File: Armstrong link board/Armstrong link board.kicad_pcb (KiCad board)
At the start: 2 copper layers, 32 x 28 mm, 8 parts, among them J1 Camera, J2 Wheelson, J3 Armstrong, J4 Conn_01x03_Pin, J5 JST 2.0, J6 USB_C_Receptacle_USB2.0_16P

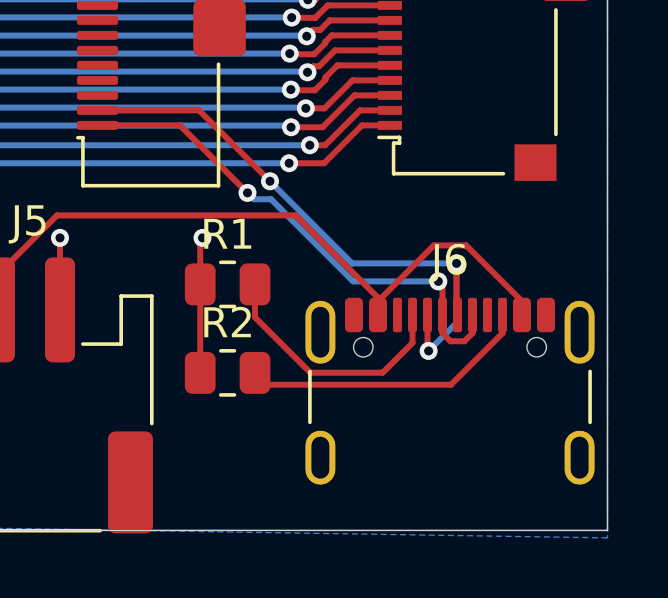
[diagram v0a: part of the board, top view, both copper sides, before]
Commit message: connect ground and shield from usb
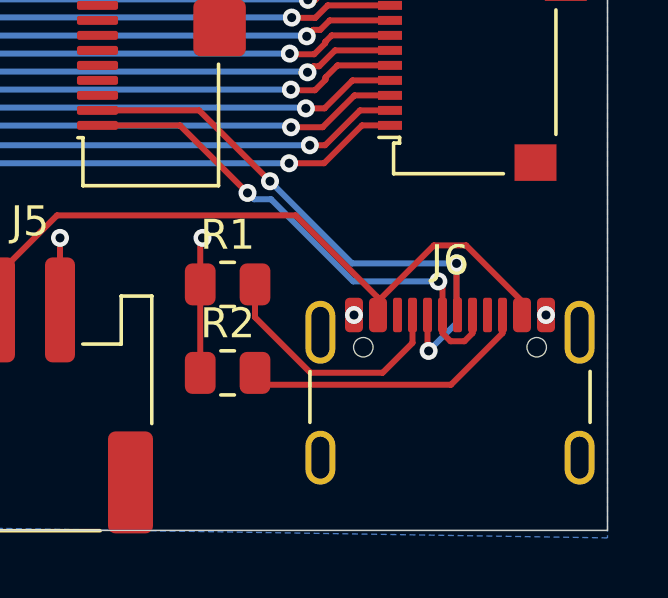
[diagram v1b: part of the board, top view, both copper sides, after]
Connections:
- J6 pad A1: unconnected-(J6-GND-PadA1) -> GND
- J6 pad A12: unconnected-(J6-GND-PadA1)_2 -> GND
- J6 pad B1: unconnected-(J6-GND-PadA1)_1 -> GND
- J6 pad B12: unconnected-(J6-GND-PadA1)_3 -> GND
- J6 pad S1: unconnected-(J6-SHIELD-PadS1) -> GND
- R2 pad 1: GND -> unconnected-(R2-Pad1)
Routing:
- net GND: vias 4 -> 6
